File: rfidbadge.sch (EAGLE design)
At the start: 57 parts, among them Q1 BSS123, U1 ATMEGA328P_TQFP, U2 CLRC663, Y1 27.12 MHz

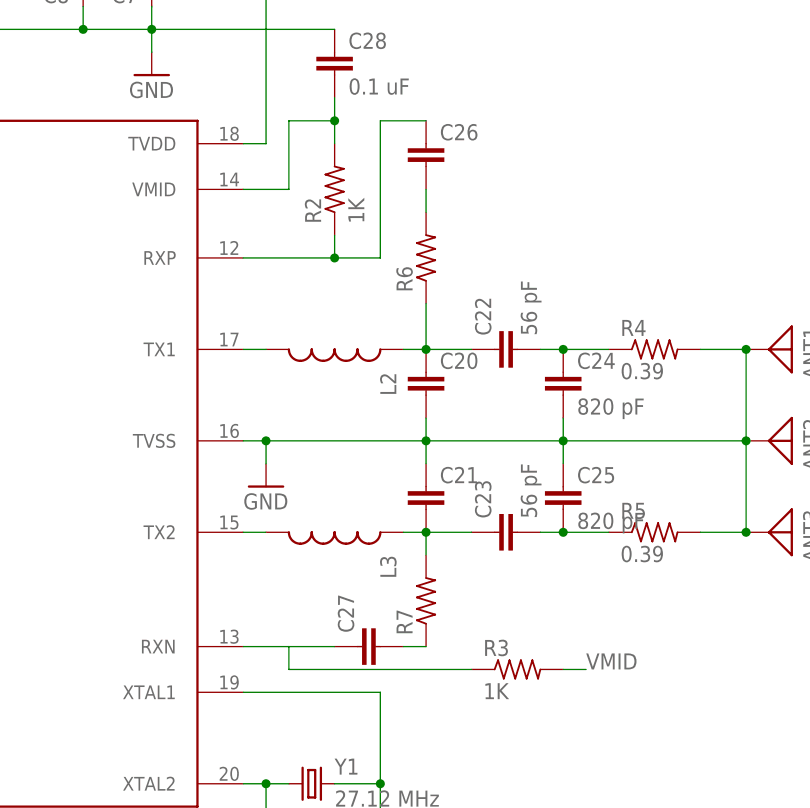
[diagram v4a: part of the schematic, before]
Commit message: Values and part numbers complete
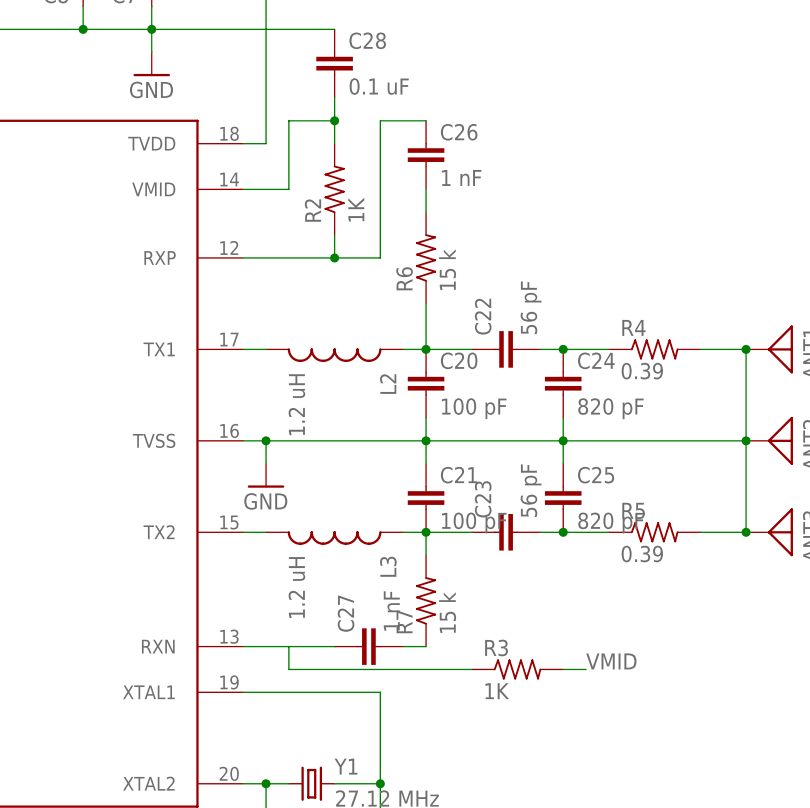
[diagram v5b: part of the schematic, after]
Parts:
- C20, C21: value (none) -> 100 pF; PROD_ID (none) -> 311-1069-1-ND
- C26, C27: value (none) -> 1 nF; PROD_ID (none) -> 311-1342-1-ND
- FTDI: PROD_ID (none) -> 952-2270-ND
- ISP: PROD_ID (none) -> 952-2121-ND
- L2, L3: value (none) -> 1.2 uH; PROD_ID (none) -> 535-12527-1-ND
- R1: PROD_ID (none) -> P56GCT-ND
- R2, R3: PROD_ID (none) -> P1.0KGCT-ND
- R6, R7: value (none) -> 15 k; PROD_ID (none) -> P15KGCT-ND
- renumbered U$1 to BAT
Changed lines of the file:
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@@
 <part name="GND7" library="supply1" deviceset="GND" device=""/>
 <part name="VDD4" library="supply1" deviceset="VDD" device=""/>
-<part name="R1" library="rcl" deviceset="R-US_" device="R0603" value="56"/>
+<part name="R1" library="rcl" deviceset="R-US_" device="R0603" value="56">
+<attribute name="PROD_ID" value="P56GCT-ND"/>
+</part>
 <part name="Q1" library="transistor-small-signal" deviceset="BSS123" device="">
 <attribute name="PROD_ID" value="2N7002ET1GOSCT-ND"/>
 </part>
 <part name="GND8" library="supply1" deviceset="GND" device=""/>
-<part name="ISP" library="pinhead" deviceset="PINHD-2X3" device=""/>
+<part name="ISP" library="pinhead" deviceset="PINHD-2X3" device="">
+<attribute name="PROD_ID" value="952-2121-ND"/>
+</part>
 <part name="VDD5" library="supply1" deviceset="VDD" device=""/>
 <part name="GND9" library="supply1" deviceset="GND" device=""/>
-<part name="FTDI" library="pinhead" deviceset="PINHD-1X6" device=""/>
+<part name="FTDI" library="pinhead" deviceset="PINHD-1X6" device="">
+<attribute name="PROD_ID" value="952-2270-ND"/>
+</part>
 <part name="C19" library="rcl" deviceset="C-EU" device="C0603K" value="0.1 uF">
 <attribute name="PROD_ID" value="311-1088-1-ND"/>
 </part>
-<part name="R2" library="rcl" deviceset="R-US_" device="R0603" value="1K"/>
-<part name="R3" library="rcl" deviceset="R-US_" device="R0603" value="1K"/>
-<part name="L2" library="SparkFun-Passives" deviceset="INDUCTOR" device="30OHM,1.8A"/>
-<part name="L3" library="SparkFun-Passives" deviceset="INDUCTOR" device="30OHM,1.8A"/>
-<part name="C20" library="rcl" deviceset="C-EU" device="C0603K">
-<attribute name="PROD_ID" value=""/>
-</part>
-<part name="C21" library="rcl" deviceset="C-EU" device="C0603K">
-<attribute name="PROD_ID" value=""/>
+<part name="R2" library="rcl" deviceset="R-US_" device="R0603" value="1K">
+<attribute name="PROD_ID" value="P1.0KGCT-ND"/>
+</part>
+<part name="R3" library="rcl" deviceset="R-US_" device="R0603" value="1K">
+<attribute name="PROD_ID" value="P1.0KGCT-ND"/>
+</part>
+<part name="L2" library="SparkFun-Passives" deviceset="INDUCTOR" device="30OHM,1.8A" value="1.2 uH">
+<attribute name="PROD_ID" value="535-12527-1-ND"/>
+</part>
+<part name="L3" library="SparkFun-Passives" deviceset="INDUCTOR" device="30OHM,1.8A" value="1.2 uH">
+<attribute name="PROD_ID" value="535-12527-1-ND"/>
+</part>
+<part name="C20" library="rcl" deviceset="C-EU" device="C0603K" value="100 pF">
+<attribute name="PROD_ID" value="311-1069-1-ND"/>
+</part>
+<part name="C21" library="rcl" deviceset="C-EU" device="C0603K" value="100 pF">
+<attribute name="PROD_ID" value="311-1069-1-ND"/>
 </part>
 <part name="C22" library="rcl" deviceset="C-EU" device="C0603K" value="56 pF">
@@
 <part name="ANT2" library="discrete" deviceset="ANTENNA" device=""/>
 <part name="ANT3" library="discrete" deviceset="ANTENNA" device=""/>
-<part name="R6" library="rcl" deviceset="R-US_" device="R0603"/>
-<part name="R7" library="rcl" deviceset="R-US_" device="R0603"/>
-<part name="C26" library="rcl" deviceset="C-EU" device="C0603K">
-<attribute name="PROD_ID" value=""/>
-</part>
-<part name="C27" library="rcl" deviceset="C-EU" device="C0603K">
-<attribute name="PROD_ID" value=""/>
+<part name="R6" library="rcl" deviceset="R-US_" device="R0603" value="15 k">
+<attribute name="PROD_ID" value="P15KGCT-ND"/>
+</part>
+<part name="R7" library="rcl" deviceset="R-US_" device="R0603" value="15 k">
+<attribute name="PROD_ID" value="P15KGCT-ND"/>
+</part>
+<part name="C26" library="rcl" deviceset="C-EU" device="C0603K" value="1 nF">
+<attribute name="PROD_ID" value="311-1342-1-ND"/>
+</part>
+<part name="C27" library="rcl" deviceset="C-EU" device="C0603K" value="1 nF">
+<attribute name="PROD_ID" value="311-1342-1-ND"/>
 </part>
 <part name="C28" library="rcl" deviceset="C-EU" device="C0603K" value="0.1 uF">
 <attribute name="PROD_ID" value="311-1088-1-ND"/>
 </part>
-<part name="U$1" library="battery_holder" deviceset="AAA_X3" device="">
+<part name="BAT" library="battery_holder" deviceset="AAA_X3" device="">
 <attribute name="PROD_ID" value="36-2479-ND"/>
 </part>
@@
 <instance part="GND7" gate="1" x="2.54" y="45.72"/>
 <instance part="VDD4" gate="G$1" x="-30.48" y="83.82"/>
-<instance part="R1" gate="G$1" x="-30.48" y="66.04" rot="R90"/>
+<instance part="R1" gate="G$1" x="-30.48" y="66.04" rot="R90">
+<attribute name="PROD_ID" x="-30.48" y="66.04" size="1.778" layer="96" rot="R90" display="off"/>
+</instance>
 <instance part="Q1" gate="G$1" x="-30.48" y="53.34">
 <attribute name="PROD_ID" x="-30.48" y="53.34" size="1.778" layer="96" display="off"/>
 </instance>
 <instance part="GND8" gate="1" x="-30.48" y="43.18"/>
-<instance part="ISP" gate="A" x="-15.24" y="-50.8"/>
+<instance part="ISP" gate="A" x="-15.24" y="-50.8">
+<attribute name="PROD_ID" x="-15.24" y="-50.8" size="1.778" layer="96" display="off"/>
+</instance>
 <instance part="VDD5" gate="G$1" x="-2.54" y="-43.18"/>
 <instance part="GND9" gate="1" x="-2.54" y="-58.42"/>
-<instance part="FTDI" gate="A" x="33.02" y="-55.88"/>
+<instance part="FTDI" gate="A" x="33.02" y="-55.88">
+<attribute name="PROD_ID" x="33.02" y="-55.88" size="1.778" layer="96" display="off"/>
+</instance>
 <instance part="C19" gate="G$1" x="7.62" y="-50.8">
 <attribute name="PROD_ID" x="7.62" y="-50.8" size="1.778" layer="96" display="off"/>
 </instance>
-<instance part="R2" gate="G$1" x="129.54" y="27.94" rot="R90"/>
-<instance part="R3" gate="G$1" x="149.86" y="-25.4"/>
+<instance part="R2" gate="G$1" x="129.54" y="27.94" rot="R90">
+<attribute name="PROD_ID" x="129.54" y="27.94" size="1.778" layer="96" rot="R90" display="off"/>
+</instance>
+<instance part="R3" gate="G$1" x="149.86" y="-25.4">
+<attribute name="PROD_ID" x="149.86" y="-25.4" size="1.778" layer="96" display="off"/>
+</instance>
 <instance part="L2" gate="G$1" x="129.54" y="10.16" rot="R270"/>
 <instance part="L3" gate="G$1" x="129.54" y="-10.16" rot="R270"/>
@@
 <instance part="ANT2" gate="A" x="180.34" y="0" rot="R270"/>
 <instance part="ANT3" gate="A" x="180.34" y="-10.16" rot="R270"/>
-<instance part="R6" gate="G$1" x="139.7" y="20.32" rot="R90"/>
-<instance part="R7" gate="G$1" x="139.7" y="-17.78" rot="R90"/>
+<instance part="R6" gate="G$1" x="139.7" y="20.32" rot="R90">
+<attribute name="PROD_ID" x="139.7" y="20.32" size="1.778" layer="96" rot="R90" display="off"/>
+</instance>
+<instance part="R7" gate="G$1" x="139.7" y="-17.78" rot="R90">
+<attribute name="PROD_ID" x="139.7" y="-17.78" size="1.778" layer="96" rot="R90" display="off"/>
+</instance>
 <instance part="C26" gate="G$1" x="139.7" y="33.02">
 <attribute name="PROD_ID" x="139.7" y="33.02" size="1.778" layer="96" display="off"/>
@@
 <attribute name="PROD_ID" x="129.54" y="43.18" size="1.778" layer="96" display="off"/>
 </instance>
-<instance part="U$1" gate="G$1" x="91.44" y="76.2">
+<instance part="BAT" gate="G$1" x="91.44" y="76.2">
 <attribute name="PROD_ID" x="91.44" y="76.2" size="1.778" layer="96" display="off"/>
 </instance>
@@
 </segment>
 <segment>
-<pinref part="U$1" gate="G$1" pin="P$1"/>
+<pinref part="BAT" gate="G$1" pin="P$1"/>
 <pinref part="GND10" gate="1" pin="GND"/>
 <wire x1="91.44" y1="71.12" x2="91.44" y2="68.58" width="0.1524" layer="91"/>
@@
 <segment>
 <pinref part="VDD6" gate="G$1" pin="VDD"/>
-<pinref part="U$1" gate="G$1" pin="P$2"/>
+<pinref part="BAT" gate="G$1" pin="P$2"/>
 <wire x1="91.44" y1="86.36" x2="91.44" y2="83.82" width="0.1524" layer="91"/>
 </segment>

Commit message: Switch part number
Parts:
- S1, S2: PROD_ID (none) -> CKN9112CT-ND
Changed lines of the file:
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@@
 <part name="GND10" library="supply1" deviceset="GND" device=""/>
 <part name="VDD6" library="supply1" deviceset="VDD" device=""/>
-<part name="S1" library="SparkFun-Electromechanical" deviceset="SWITCH-MOMENTARY-2" device="SMD-4"/>
-<part name="S2" library="SparkFun-Electromechanical" deviceset="SWITCH-MOMENTARY-2" device="SMD-4"/>
+<part name="S1" library="SparkFun-Electromechanical" deviceset="SWITCH-MOMENTARY-2" device="SMD-4">
+<attribute name="PROD_ID" value="CKN9112CT-ND"/>
+</part>
+<part name="S2" library="SparkFun-Electromechanical" deviceset="SWITCH-MOMENTARY-2" device="SMD-4">
+<attribute name="PROD_ID" value="CKN9112CT-ND"/>
+</part>
 <part name="GND11" library="supply1" deviceset="GND" device=""/>
 <part name="TP1" library="testpad" deviceset="TP" device="TP06R" value="TPTP06R"/>

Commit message: s/CLRC633/CLRC663/
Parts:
- U2: device CLRC633:CLRC663 -> CLRC663:CLRC663
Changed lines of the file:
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@@
 <attribute name="PROD_ID" value="ATMEGA328PB-AURCT-ND"/>
 </part>
-<part name="U2" library="CLRC633" deviceset="CLRC663" device="">
+<part name="U2" library="CLRC663" deviceset="CLRC663" device="">
 <attribute name="PROD_ID" value="568-11528-ND"/>
 </part>

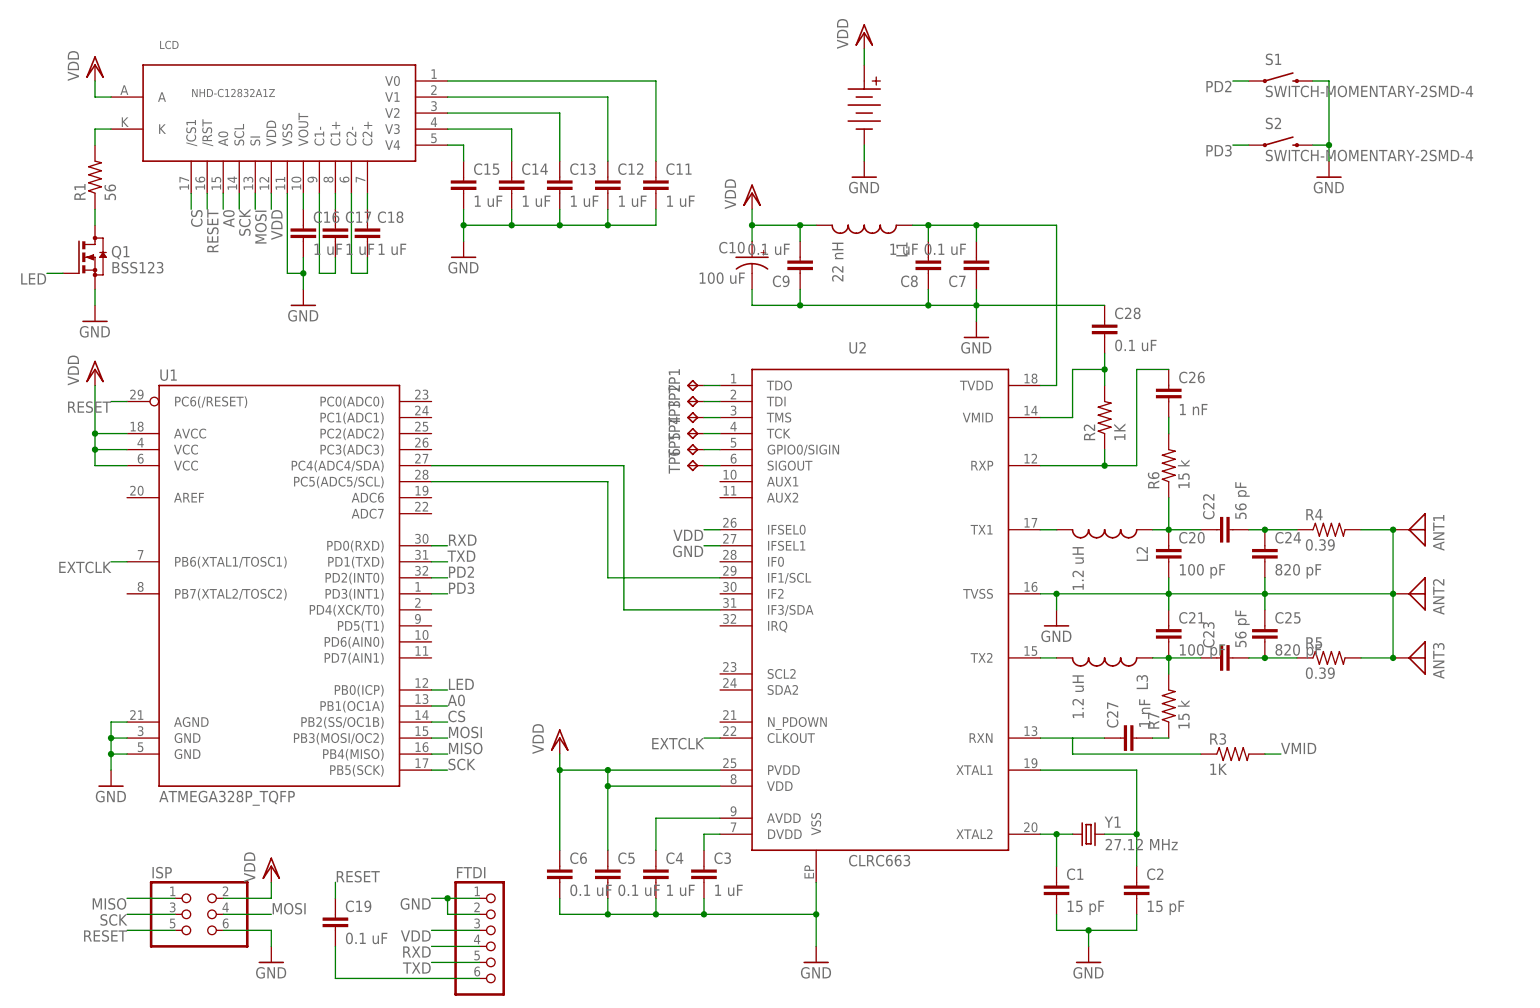
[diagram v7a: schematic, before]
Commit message: Connect IRQ line, move buttons
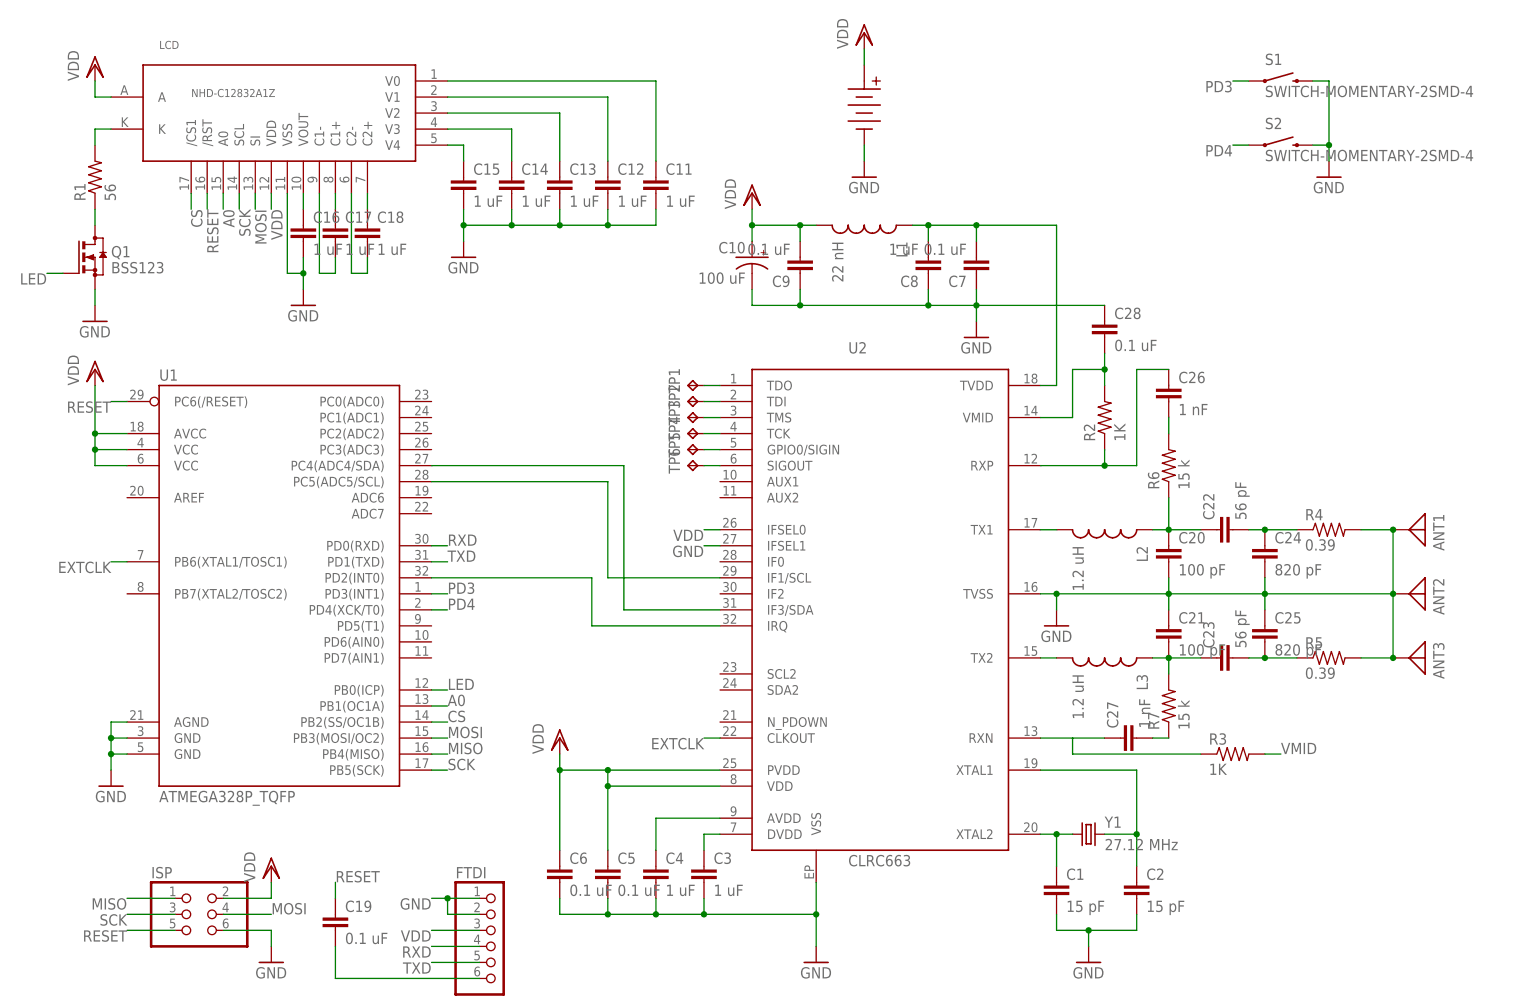
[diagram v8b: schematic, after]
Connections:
- new net PD4: S2.1, U1.PD4(XCK/T0)
- net PD2: now also U2.IRQ; no longer S1.1
- net PD3: now also S1.1; no longer S2.1
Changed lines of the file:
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@@
 <segment>
 <pinref part="U1" gate="U$1" pin="PD2(INT0)"/>
-<wire x1="22.86" y1="2.54" x2="25.4" y2="2.54" width="0.1524" layer="91"/>
-<label x="25.4" y="2.54" size="1.778" layer="95"/>
-</segment>
-<segment>
-<pinref part="S1" gate="G$1" pin="1"/>
-<wire x1="152.4" y1="81.28" x2="149.86" y2="81.28" width="0.1524" layer="91"/>
-<label x="149.86" y="81.28" size="1.778" layer="95" rot="R180"/>
-</segment>
-</net>
-<net name="PD3" class="0">
-<segment>
-<pinref part="U1" gate="U$1" pin="PD3(INT1)"/>
-<wire x1="22.86" y1="0" x2="25.4" y2="0" width="0.1524" layer="91"/>
-<label x="25.4" y="0" size="1.778" layer="95"/>
-</segment>
-<segment>
-<pinref part="S2" gate="G$1" pin="1"/>
-<wire x1="152.4" y1="71.12" x2="149.86" y2="71.12" width="0.1524" layer="91"/>
-<label x="149.86" y="71.12" size="1.778" layer="95" rot="R180"/>
+<pinref part="U2" gate="G$1" pin="IRQ"/>
+<wire x1="68.58" y1="-5.08" x2="48.26" y2="-5.08" width="0.1524" layer="91"/>
+<wire x1="48.26" y1="-5.08" x2="48.26" y2="2.54" width="0.1524" layer="91"/>
+<wire x1="48.26" y1="2.54" x2="22.86" y2="2.54" width="0.1524" layer="91"/>
 </segment>
 </net>
@@
 </segment>
 </net>
+<net name="PD4" class="0">
+<segment>
+<pinref part="U1" gate="U$1" pin="PD4(XCK/T0)"/>
+<wire x1="22.86" y1="-2.54" x2="25.4" y2="-2.54" width="0.1524" layer="91"/>
+<label x="25.4" y="-2.54" size="1.778" layer="95"/>
+</segment>
+<segment>
+<pinref part="S2" gate="G$1" pin="1"/>
+<wire x1="152.4" y1="71.12" x2="149.86" y2="71.12" width="0.1524" layer="91"/>
+<label x="149.86" y="71.12" size="1.778" layer="95" rot="R180"/>
+</segment>
+</net>
+<net name="PD3" class="0">
+<segment>
+<pinref part="U1" gate="U$1" pin="PD3(INT1)"/>
+<wire x1="22.86" y1="0" x2="25.4" y2="0" width="0.1524" layer="91"/>
+<label x="25.4" y="0" size="1.778" layer="95"/>
+</segment>
+<segment>
+<pinref part="S1" gate="G$1" pin="1"/>
+<wire x1="152.4" y1="81.28" x2="149.86" y2="81.28" width="0.1524" layer="91"/>
+<label x="149.86" y="81.28" size="1.778" layer="95" rot="R180"/>
+</segment>
+</net>
